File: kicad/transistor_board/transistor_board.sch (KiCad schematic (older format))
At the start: 16 parts, among them J1 Conn_01x10, J2 Conn_01x02, Q1 MMBF170, Q2 MMBF170, Q3 MMBF170, Q4 MMBF170, U2 ESP32-cam, U3 LM7805_TO220

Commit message: added footprints
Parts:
- C3, C4, C5, C6: footprint (none) -> Capacitor_SMD:C_01005_0402Metric
- D1: footprint (none) -> Diode_SMD:Diode_Bridge_Vishay_DFS
- J1: footprint kicad:Molex_KK-254_AE-6410-10A_1x10_P2.54mm_Vertical -> Connector_PinHeader_2.54mm:PinHeader_1x10_P2.54mm_Vertical
- J2: footprint (none) -> Connector_PinHeader_2.54mm:PinHeader_1x02_P2.54mm_Vertical
- R1: footprint (none) -> Resistor_SMD:R_2512_6332Metric
- U2: footprint (none) -> transistor_board:ESP32-CAM
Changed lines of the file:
@@
 F 0 "U2" H 7150 2115 50  0000 C CNN
 F 1 "ESP32-cam" H 7150 2024 50  0000 C CNN
-F 2 "" H 6300 3100 50  0001 C CNN
+F 2 "transistor_board:ESP32-CAM" H 6300 3100 50  0001 C CNN
 F 3 "" H 6300 3100 50  0001 C CNN
 	1    7150 1450
@@
 F 0 "D1" H 5244 2546 50  0000 L CNN
 F 1 "D_Bridge_+-AA" H 5244 2455 50  0000 L CNN
-F 2 "" H 4900 2500 50  0001 C CNN
+F 2 "Diode_SMD:Diode_Bridge_Vishay_DFS" H 4900 2500 50  0001 C CNN
 F 3 "~" H 4900 2500 50  0001 C CNN
 	1    4900 2500
@@
 F 0 "R1" V 4800 3800 50  0000 L CNN
 F 1 "R" V 4900 3850 50  0000 L CNN
-F 2 "" V 4830 3850 50  0001 C CNN
+F 2 "Resistor_SMD:R_2512_6332Metric" V 4830 3850 50  0001 C CNN
 F 3 "~" H 4900 3850 50  0001 C CNN
 	1    4900 3850
@@
 F 0 "C4" H 5265 1146 50  0000 L CNN
 F 1 "C" H 5265 1055 50  0000 L CNN
-F 2 "" H 5188 950 50  0001 C CNN
+F 2 "Capacitor_SMD:C_01005_0402Metric" H 5188 950 50  0001 C CNN
 F 3 "~" H 5150 1100 50  0001 C CNN
 	1    5150 1100
@@
 F 0 "C5" H 8915 1196 50  0000 L CNN
 F 1 "C" H 8915 1105 50  0000 L CNN
-F 2 "" H 8838 1000 50  0001 C CNN
+F 2 "Capacitor_SMD:C_01005_0402Metric" H 8838 1000 50  0001 C CNN
 F 3 "~" H 8800 1150 50  0001 C CNN
 	1    8800 1150
@@
 F 0 "C3" V 4750 1950 50  0000 C CNN
 F 1 "C" V 5050 1950 50  0000 C CNN
-F 2 "" H 4938 1800 50  0001 C CNN
+F 2 "Capacitor_SMD:C_01005_0402Metric" H 4938 1800 50  0001 C CNN
 F 3 "~" H 4900 1950 50  0001 C CNN
 	1    4900 1950
@@
 F 0 "C6" V 3398 1050 50  0000 C CNN
 F 1 "C" V 3489 1050 50  0000 C CNN
-F 2 "" H 3688 900 50  0001 C CNN
+F 2 "Capacitor_SMD:C_01005_0402Metric" H 3688 900 50  0001 C CNN
 F 3 "~" H 3650 1050 50  0001 C CNN
 	1    3650 1050
@@
 F 0 "J1" H 3368 2825 50  0000 C CNN
 F 1 "Conn_01x10" H 3368 2916 50  0000 C CNN
-F 2 "kicad:Molex_KK-254_AE-6410-10A_1x10_P2.54mm_Vertical" H 3450 3550 50  0001 C CNN
+F 2 "Connector_PinHeader_2.54mm:PinHeader_1x10_P2.54mm_Vertical" H 3450 3550 50  0001 C CNN
 F 3 "~" H 3450 3550 50  0001 C CNN
 	1    3450 3550
@@
 F 0 "J2" H 7618 2675 50  0000 C CNN
 F 1 "Conn_01x02" H 7618 2766 50  0000 C CNN
-F 2 "" H 7700 3000 50  0001 C CNN
+F 2 "Connector_PinHeader_2.54mm:PinHeader_1x02_P2.54mm_Vertical" H 7700 3000 50  0001 C CNN
 F 3 "~" H 7700 3000 50  0001 C CNN
 	1    7700 3000

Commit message: updated for newer libraries
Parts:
- C3, C4, C5, C6: symbol Device:C -> transistor_board-rescue:C-Device
- D1: symbol Device:D_Bridge_+-AA -> transistor_board-rescue:D_Bridge_+-AA-Device
- D2, D3: symbol Device:D_x2_KCom_AAK -> transistor_board-rescue:D_x2_KCom_AAK-Device
- J1: symbol Connector_Generic:Conn_01x10 -> transistor_board-rescue:Conn_01x10-Connector_Generic
- J2: symbol Connector_Generic:Conn_01x02 -> transistor_board-rescue:Conn_01x02-Connector_Generic
- Q1, Q2, Q3, Q4: symbol Transistor_FET:MMBF170 -> transistor_board-rescue:MMBF170-Transistor_FET
- R1: symbol Device:R -> transistor_board-rescue:R-Device
- U3: symbol Regulator_Linear:LM7805_TO220 -> transistor_board-rescue:LM7805_TO220-Regulator_Linear
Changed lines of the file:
@@
 $EndComp
 $Comp
-L Device:D_Bridge_+-AA D1
+L transistor_board-rescue:D_Bridge_+-AA-Device D1
 U 1 1 5F218132
 P 4900 2500
@@
 	4550 3950 4000 3950
 $Comp
-L power:GND #PWR03
+L transistor_board-rescue:GND-power #PWR03
 U 1 1 5F21C64D
 P 4000 4200
@@
 	5200 2500 5400 2500
 $Comp
-L Device:R R1
+L transistor_board-rescue:R-Device R1
 U 1 1 5F21E564
 P 4900 3850
@@
 	6600 1250 5800 1250
 $Comp
-L Transistor_FET:MMBF170 Q4
+L transistor_board-rescue:MMBF170-Transistor_FET Q4
 U 1 1 5F2578EE
 P 7150 3750
@@
 	6500 3750 6950 3750
 $Comp
-L power:GND #PWR06
+L transistor_board-rescue:GND-power #PWR06
 U 1 1 5F260D53
 P 7250 3050
@@
 $EndComp
 $Comp
-L power:GND #PWR07
+L transistor_board-rescue:GND-power #PWR07
 U 1 1 5F261517
 P 7250 4050
@@
 	7250 3450 6600 3450
 $Comp
-L Transistor_FET:MMBF170 Q3
+L transistor_board-rescue:MMBF170-Transistor_FET Q3
 U 1 1 5F2BA0E0
 P 7150 4700
@@
 	6300 4700 6950 4700
 $Comp
-L power:GND #PWR08
+L transistor_board-rescue:GND-power #PWR08
 U 1 1 5F2CD5B4
 P 7250 5000
@@
 Connection ~ 5400 2500
 $Comp
-L power:GND #PWR09
+L transistor_board-rescue:GND-power #PWR09
 U 1 1 5F2E15CA
 P 5600 1300
@@
 	5600 1150 6600 1150
 $Comp
-L Device:C C4
+L transistor_board-rescue:C-Device C4
 U 1 1 5F2E553A
 P 5150 1100
@@
 	5450 1050 6600 1050
 $Comp
-L Regulator_Linear:LM7805_TO220 U3
+L transistor_board-rescue:LM7805_TO220-Regulator_Linear U3
 U 1 1 5F300908
 P 4550 850
@@
 $EndComp
 $Comp
-L Device:C C5
+L transistor_board-rescue:C-Device C5
 U 1 1 5F3038BA
 P 8800 1150
@@
 $EndComp
 $Comp
-L power:GND #PWR010
+L transistor_board-rescue:GND-power #PWR010
 U 1 1 5F3049EF
 P 8800 1400
@@
 Connection ~ 8050 900
 $Comp
-L power:GND #PWR011
+L transistor_board-rescue:GND-power #PWR011
 U 1 1 5F30F2B4
 P 4550 1250
@@
 	4550 1150 4550 1250
 $Comp
-L Device:C C3
+L transistor_board-rescue:C-Device C3
 U 1 1 5F313280
 P 4900 1950
@@
 	4150 850  4150 3850
 $Comp
-L Device:C C6
+L transistor_board-rescue:C-Device C6
 U 1 1 5F24F95F
 P 3650 1050
@@
 Connection ~ 4150 850
 $Comp
-L power:GND #PWR012
+L transistor_board-rescue:GND-power #PWR012
 U 1 1 5F253D6E
 P 3650 1300
@@
 	4000 3750 3650 3750
 $Comp
-L Transistor_FET:MMBF170 Q2
+L transistor_board-rescue:MMBF170-Transistor_FET Q2
 U 1 1 5F261E90
 P 9050 3250
@@
 $EndComp
 $Comp
-L Transistor_FET:MMBF170 Q1
+L transistor_board-rescue:MMBF170-Transistor_FET Q1
 U 1 1 5F263B9D
 P 9050 4150
@@
 	8700 3250 8850 3250
 $Comp
-L power:GND #PWR02
+L transistor_board-rescue:GND-power #PWR02
 U 1 1 5F2F30E0
 P 9150 4450
@@
 $EndComp
 $Comp
-L power:GND #PWR01
+L transistor_board-rescue:GND-power #PWR01
 U 1 1 5F2F3C1D
 P 9150 3550
@@
 	6600 1650 6200 1650
 $Comp
-L Connector_Generic:Conn_01x10 J1
+L transistor_board-rescue:Conn_01x10-Connector_Generic J1
 U 1 1 5F26F492
 P 3450 3550
@@
 $EndComp
 $Comp
-L Device:D_x2_KCom_AAK D3
+L transistor_board-rescue:D_x2_KCom_AAK-Device D3
 U 1 1 5F27964B
 P 9800 1800
@@
 	9350 2900 10200 2900
 $Comp
-L Device:D_x2_KCom_AAK D2
+L transistor_board-rescue:D_x2_KCom_AAK-Device D2
 U 1 1 5F29965A
 P 8150 5200
@@
 	8500 3450 8500 5200
 $Comp
-L Connector_Generic:Conn_01x02 J2
+L transistor_board-rescue:Conn_01x02-Connector_Generic J2
 U 1 1 5F30B63D
 P 7700 3000

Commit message: changed some footprints
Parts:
- C3, C4, C5, C6: footprint Capacitor_SMD:C_01005_0402Metric -> Capacitor_SMD:C_0805_2012Metric
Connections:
- net at U2.4 (IO4): now also Q2.1 (G)
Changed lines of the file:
@@
 F 0 "C4" H 5265 1146 50  0000 L CNN
 F 1 "C" H 5265 1055 50  0000 L CNN
-F 2 "Capacitor_SMD:C_01005_0402Metric" H 5188 950 50  0001 C CNN
+F 2 "Capacitor_SMD:C_0805_2012Metric" H 5188 950 50  0001 C CNN
 F 3 "~" H 5150 1100 50  0001 C CNN
 	1    5150 1100
@@
 F 0 "C5" H 8915 1196 50  0000 L CNN
 F 1 "C" H 8915 1105 50  0000 L CNN
-F 2 "Capacitor_SMD:C_01005_0402Metric" H 8838 1000 50  0001 C CNN
+F 2 "Capacitor_SMD:C_0805_2012Metric" H 8838 1000 50  0001 C CNN
 F 3 "~" H 8800 1150 50  0001 C CNN
 	1    8800 1150
@@
 F 0 "C3" V 4750 1950 50  0000 C CNN
 F 1 "C" V 5050 1950 50  0000 C CNN
-F 2 "Capacitor_SMD:C_01005_0402Metric" H 4938 1800 50  0001 C CNN
+F 2 "Capacitor_SMD:C_0805_2012Metric" H 4938 1800 50  0001 C CNN
 F 3 "~" H 4900 1950 50  0001 C CNN
 	1    4900 1950
@@
 F 0 "C6" V 3398 1050 50  0000 C CNN
 F 1 "C" V 3489 1050 50  0000 C CNN
-F 2 "Capacitor_SMD:C_01005_0402Metric" H 3688 900 50  0001 C CNN
+F 2 "Capacitor_SMD:C_0805_2012Metric" H 3688 900 50  0001 C CNN
 F 3 "~" H 3650 1050 50  0001 C CNN
 	1    3650 1050

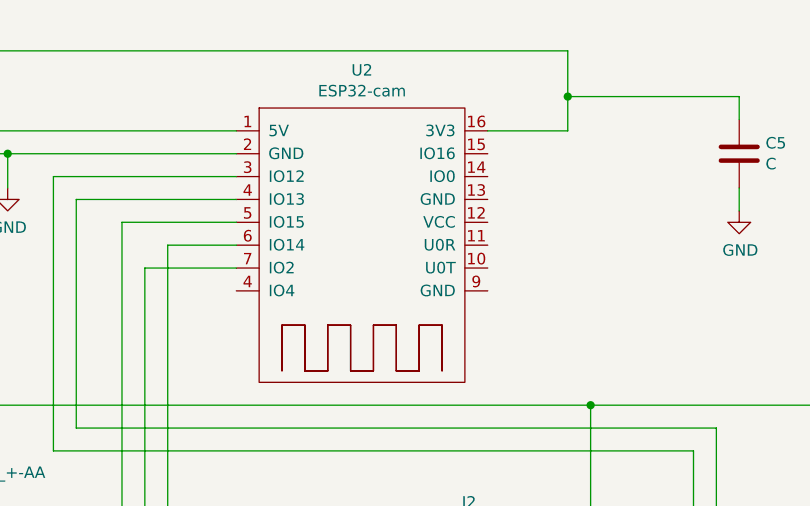
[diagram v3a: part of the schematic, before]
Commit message: made cut out for connecting serial port
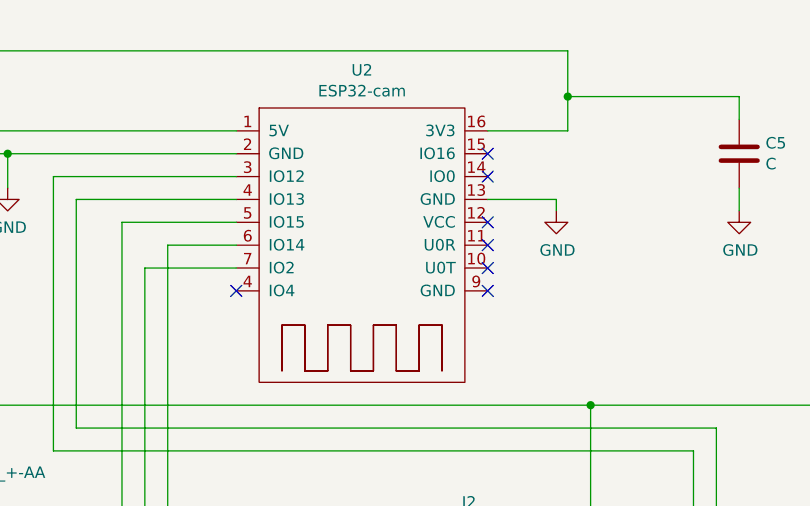
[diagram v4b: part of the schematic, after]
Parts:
- U2: footprint transistor_board:ESP32-CAM -> eit_footprints:ESP32-CAM_12pin
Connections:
- net GND: now also U2.13 (GND)
- net at U2.4 (IO4): now also Q2.1 (G)
- no-connect marks 0 -> 7
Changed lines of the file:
@@
 Sheet 1 1
 Title ""
-Date "2020-07-29"
+Date "2020-08-16"
 Rev ""
 Comp ""
@@
 F 0 "U2" H 7150 2115 50  0000 C CNN
 F 1 "ESP32-cam" H 7150 2024 50  0000 C CNN
-F 2 "transistor_board:ESP32-CAM" H 6300 3100 50  0001 C CNN
+F 2 "eit_footprints:ESP32-CAM_12pin" H 6300 3100 50  0001 C CNN
 F 3 "" H 6300 3100 50  0001 C CNN
 	1    7150 1450
@@
 Wire Wire Line
 	6200 2900 7500 2900
+$Comp
+L transistor_board-rescue:GND-power #PWR?
+U 1 1 5F39AC86
+P 8000 1400
+F 0 "#PWR?" H 8000 1150 50  0001 C CNN
+F 1 "GND" H 8005 1227 50  0000 C CNN
+F 2 "" H 8000 1400 50  0001 C CNN
+F 3 "" H 8000 1400 50  0001 C CNN
+	1    8000 1400
+	1    0    0    -1
+$EndComp
+Wire Wire Line
+	8000 1400 8000 1350
+Wire Wire Line
+	8000 1350 7700 1350
+NoConn ~ 6600 1750
+NoConn ~ 7700 1250
+NoConn ~ 7700 1150
+NoConn ~ 7700 1450
+NoConn ~ 7700 1550
+NoConn ~ 7700 1650
+NoConn ~ 7700 1750
 $EndSCHEMATC

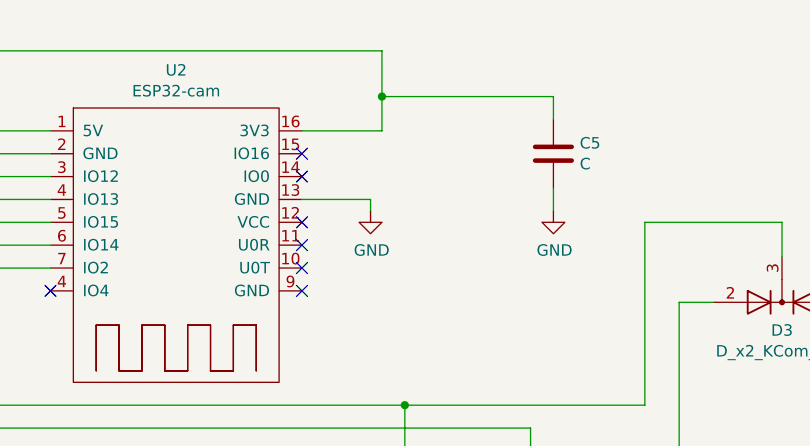
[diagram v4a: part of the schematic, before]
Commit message: remember: To enable download connect GPIO0/IO0 to GND.
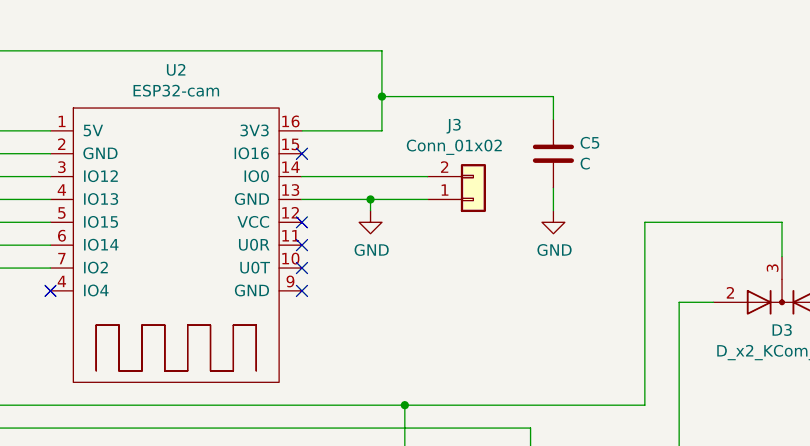
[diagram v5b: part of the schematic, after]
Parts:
- added J3: Conn_01x02, Connector_PinHeader_2.54mm:PinHeader_1x02_P2.54mm_Vertical, symbol transistor_board-rescue:Conn_01x02-Connector_Generic
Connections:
- net GND: now also J3.1 (Pin_1)
- net at U2.14 (IO0): now also J3.2 (Pin_2)
- net at U2.4 (IO4): now also Q2.1 (G)
- no-connect marks 7 -> 6
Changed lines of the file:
@@
 	6200 2900 7500 2900
 $Comp
-L transistor_board-rescue:GND-power #PWR?
+L transistor_board-rescue:GND-power #PWR04
 U 1 1 5F39AC86
 P 8000 1400
-F 0 "#PWR?" H 8000 1150 50  0001 C CNN
+F 0 "#PWR04" H 8000 1150 50  0001 C CNN
 F 1 "GND" H 8005 1227 50  0000 C CNN
 F 2 "" H 8000 1400 50  0001 C CNN
@@
 	8000 1350 7700 1350
 NoConn ~ 6600 1750
-NoConn ~ 7700 1250
 NoConn ~ 7700 1150
 NoConn ~ 7700 1450
@@
 NoConn ~ 7700 1650
 NoConn ~ 7700 1750
+$Comp
+L transistor_board-rescue:Conn_01x02-Connector_Generic J3
+U 1 1 5F39F718
+P 8450 1350
+F 0 "J3" H 8368 1025 50  0000 C CNN
+F 1 "Conn_01x02" H 8368 1116 50  0000 C CNN
+F 2 "Connector_PinHeader_2.54mm:PinHeader_1x02_P2.54mm_Vertical" H 8450 1350 50  0001 C CNN
+F 3 "~" H 8450 1350 50  0001 C CNN
+	1    8450 1350
+	1    0    0    1
+$EndComp
+Wire Wire Line
+	8250 1350 8000 1350
+Connection ~ 8000 1350
+Wire Wire Line
+	8250 1250 7700 1250
 $EndSCHEMATC

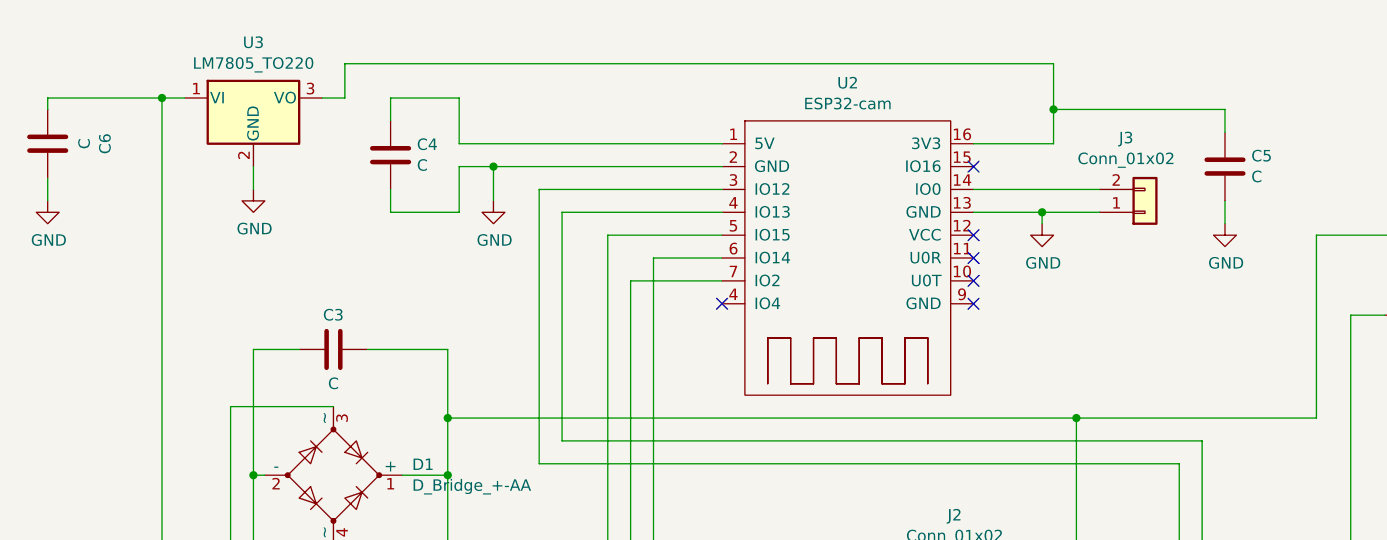
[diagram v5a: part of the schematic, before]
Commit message: Transistors failed, need to use bigger, such as D-Pak (TO252AA)
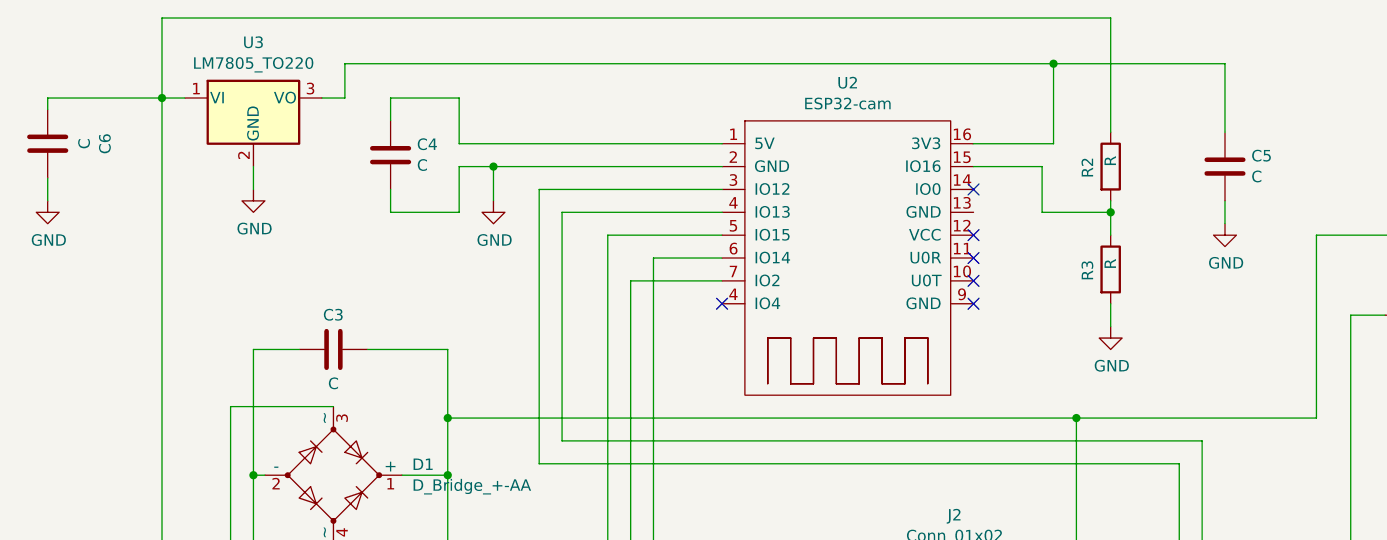
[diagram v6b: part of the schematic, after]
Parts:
- removed J3: Conn_01x02, Connector_PinHeader_2.54mm:PinHeader_1x02_P2.54mm_Vertical, symbol transistor_board-rescue:Conn_01x02-Connector_Generic
- added R2, R3: R, Resistor_SMD:R_0805_2012Metric, symbol transistor_board-rescue:R-Device
- Q1, Q2: footprint Package_TO_SOT_SMD:SOT-23 -> Package_TO_SOT_SMD:TO-252-3_TabPin2
- U2: footprint eit_footprints:ESP32-CAM_12pin -> eit_footprints:ESP32-CAM
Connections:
- net GND: now also R3.2; no longer U2.13 (GND)
- net at U2.15 (IO16): now also R2.2, R3.1
- net at U2.4 (IO4): now also Q2.1 (G)
- net at C6.2, J1.2 (Pin_2), R1.1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: now also R2.1
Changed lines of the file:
@@
 Sheet 1 1
 Title ""
-Date "2020-08-16"
+Date "2020-09-15"
 Rev ""
 Comp ""
@@
 F 0 "U2" H 7150 2115 50  0000 C CNN
 F 1 "ESP32-cam" H 7150 2024 50  0000 C CNN
-F 2 "eit_footprints:ESP32-CAM_12pin" H 6300 3100 50  0001 C CNN
+F 2 "eit_footprints:ESP32-CAM" H 6300 3100 50  0001 C CNN
 F 3 "" H 6300 3100 50  0001 C CNN
 	1    7150 1450
@@
 $EndComp
 Wire Wire Line
-	6200 2900 6200 1650
-Wire Wire Line
 	6600 1450 6100 1450
 Wire Wire Line
@@
 Wire Wire Line
 	6500 3750 6950 3750
-$Comp
-L transistor_board-rescue:GND-power #PWR06
-U 1 1 5F260D53
-P 7250 3050
-F 0 "#PWR06" H 7250 2800 50  0001 C CNN
-F 1 "GND" H 7255 2877 50  0000 C CNN
-F 2 "" H 7250 3050 50  0001 C CNN
-F 3 "" H 7250 3050 50  0001 C CNN
-	1    7250 3050
-	1    0    0    -1
-$EndComp
 $Comp
 L transistor_board-rescue:GND-power #PWR07
@@
 	7700 1050 8050 1050
 Wire Wire Line
-	8050 1050 8050 900
-Wire Wire Line
-	8050 900  8800 900
-Wire Wire Line
-	8800 900  8800 1000
-Wire Wire Line
-	8050 900  8050 700
+	8050 1050 8050 700
+Wire Wire Line
+	8050 700  8800 700
+Wire Wire Line
+	8800 700  8800 1000
 Wire Wire Line
 	8050 700  4950 700
@@
 Wire Wire Line
 	4950 850  4850 850
-Connection ~ 8050 900
+Connection ~ 8050 700
 $Comp
 L transistor_board-rescue:GND-power #PWR011
@@
 F 0 "Q2" H 9254 3296 50  0000 L CNN
 F 1 "MMBF170" H 9254 3205 50  0000 L CNN
-F 2 "Package_TO_SOT_SMD:SOT-23" H 9250 3175 50  0001 L CIN
+F 2 "Package_TO_SOT_SMD:TO-252-3_TabPin2" H 9250 3175 50  0001 L CIN
 F 3 "https://www.diodes.com/assets/Datasheets/ds30104.pdf" H 9050 3250 50  0001 L CNN
 	1    9050 3250
@@
 F 0 "Q1" H 9254 4196 50  0000 L CNN
 F 1 "MMBF170" H 9254 4105 50  0000 L CNN
-F 2 "Package_TO_SOT_SMD:SOT-23" H 9250 4075 50  0001 L CIN
+F 2 "Package_TO_SOT_SMD:TO-252-3_TabPin2" H 9250 4075 50  0001 L CIN
 F 3 "https://www.diodes.com/assets/Datasheets/ds30104.pdf" H 9050 4150 50  0001 L CNN
 	1    9050 4150
@@
 Wire Wire Line
 	6300 1550 6300 4700
-Wire Wire Line
-	6600 1650 6200 1650
 $Comp
 L transistor_board-rescue:Conn_01x10-Connector_Generic J1
@@
 Wire Wire Line
 	8500 3450 8500 5200
+NoConn ~ 6600 1750
+NoConn ~ 7700 1450
+NoConn ~ 7700 1550
+NoConn ~ 7700 1650
+NoConn ~ 7700 1750
+Wire Wire Line
+	6600 1650 6200 1650
+Wire Wire Line
+	6200 2900 6200 1650
+Wire Wire Line
+	6200 2900 7500 2900
+Wire Wire Line
+	7250 3000 7250 3050
+Wire Wire Line
+	7500 3000 7250 3000
 $Comp
 L transistor_board-rescue:Conn_01x02-Connector_Generic J2
@@
 	1    0    0    1
 $EndComp
-Wire Wire Line
-	7500 3000 7250 3000
-Wire Wire Line
-	7250 3000 7250 3050
-Wire Wire Line
-	6200 2900 7500 2900
+$Comp
+L transistor_board-rescue:GND-power #PWR06
+U 1 1 5F260D53
+P 7250 3050
+F 0 "#PWR06" H 7250 2800 50  0001 C CNN
+F 1 "GND" H 7255 2877 50  0000 C CNN
+F 2 "" H 7250 3050 50  0001 C CNN
+F 3 "" H 7250 3050 50  0001 C CNN
+	1    7250 3050
+	1    0    0    -1
+$EndComp
+NoConn ~ 7700 1250
+$Comp
+L transistor_board-rescue:R-Device R3
+U 1 1 5F61F0F4
+P 8300 1600
+F 0 "R3" V 8200 1550 50  0000 L CNN
+F 1 "R" V 8300 1600 50  0000 L CNN
+F 2 "Resistor_SMD:R_0805_2012Metric" V 8230 1600 50  0001 C CNN
+F 3 "~" H 8300 1600 50  0001 C CNN
+	1    8300 1600
+	1    0    0    -1
+$EndComp
+$Comp
+L transistor_board-rescue:R-Device R2
+U 1 1 5F620284
+P 8300 1150
+F 0 "R2" V 8200 1100 50  0000 L CNN
+F 1 "R" V 8300 1150 50  0000 L CNN
+F 2 "Resistor_SMD:R_0805_2012Metric" V 8230 1150 50  0001 C CNN
+F 3 "~" H 8300 1150 50  0001 C CNN
+	1    8300 1150
+	1    0    0    -1
+$EndComp
 $Comp
 L transistor_board-rescue:GND-power #PWR04
-U 1 1 5F39AC86
-P 8000 1400
-F 0 "#PWR04" H 8000 1150 50  0001 C CNN
-F 1 "GND" H 8005 1227 50  0000 C CNN
-F 2 "" H 8000 1400 50  0001 C CNN
-F 3 "" H 8000 1400 50  0001 C CNN
-	1    8000 1400
-	1    0    0    -1
-$EndComp
-Wire Wire Line
-	8000 1400 8000 1350
-Wire Wire Line
-	8000 1350 7700 1350
-NoConn ~ 6600 1750
-NoConn ~ 7700 1150
-NoConn ~ 7700 1450
-NoConn ~ 7700 1550
-NoConn ~ 7700 1650
-NoConn ~ 7700 1750
-$Comp
-L transistor_board-rescue:Conn_01x02-Connector_Generic J3
-U 1 1 5F39F718
-P 8450 1350
-F 0 "J3" H 8368 1025 50  0000 C CNN
-F 1 "Conn_01x02" H 8368 1116 50  0000 C CNN
-F 2 "Connector_PinHeader_2.54mm:PinHeader_1x02_P2.54mm_Vertical" H 8450 1350 50  0001 C CNN
-F 3 "~" H 8450 1350 50  0001 C CNN
-	1    8450 1350
-	1    0    0    1
-$EndComp
-Wire Wire Line
-	8250 1350 8000 1350
-Connection ~ 8000 1350
-Wire Wire Line
-	8250 1250 7700 1250
+U 1 1 5F62EF8E
+P 8300 1850
+F 0 "#PWR04" H 8300 1600 50  0001 C CNN
+F 1 "GND" H 8305 1677 50  0000 C CNN
+F 2 "" H 8300 1850 50  0001 C CNN
+F 3 "" H 8300 1850 50  0001 C CNN
+	1    8300 1850
+	1    0    0    -1
+$EndComp
+Wire Wire Line
+	8300 1850 8300 1750
+Wire Wire Line
+	8300 1450 8300 1350
+Wire Wire Line
+	8300 1350 8000 1350
+Wire Wire Line
+	8000 1350 8000 1150
+Wire Wire Line
+	8000 1150 7700 1150
+Connection ~ 8300 1350
+Wire Wire Line
+	8300 1350 8300 1300
+Wire Wire Line
+	4150 850  4150 500
+Wire Wire Line
+	4150 500  8300 500
+Wire Wire Line
+	8300 500  8300 1000
 $EndSCHEMATC
